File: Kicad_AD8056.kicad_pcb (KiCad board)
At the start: 2 copper layers, 63.5 x 70.9 mm, 10 parts, among them J1 Conn_Coaxial, J2 Screw_Terminal_01x03, J3 Conn_Coaxial, J4 Conn_01x01_Pin, J5 Conn_01x01_Pin, J6 Conn_01x01_Pin, U1 AD8056AR

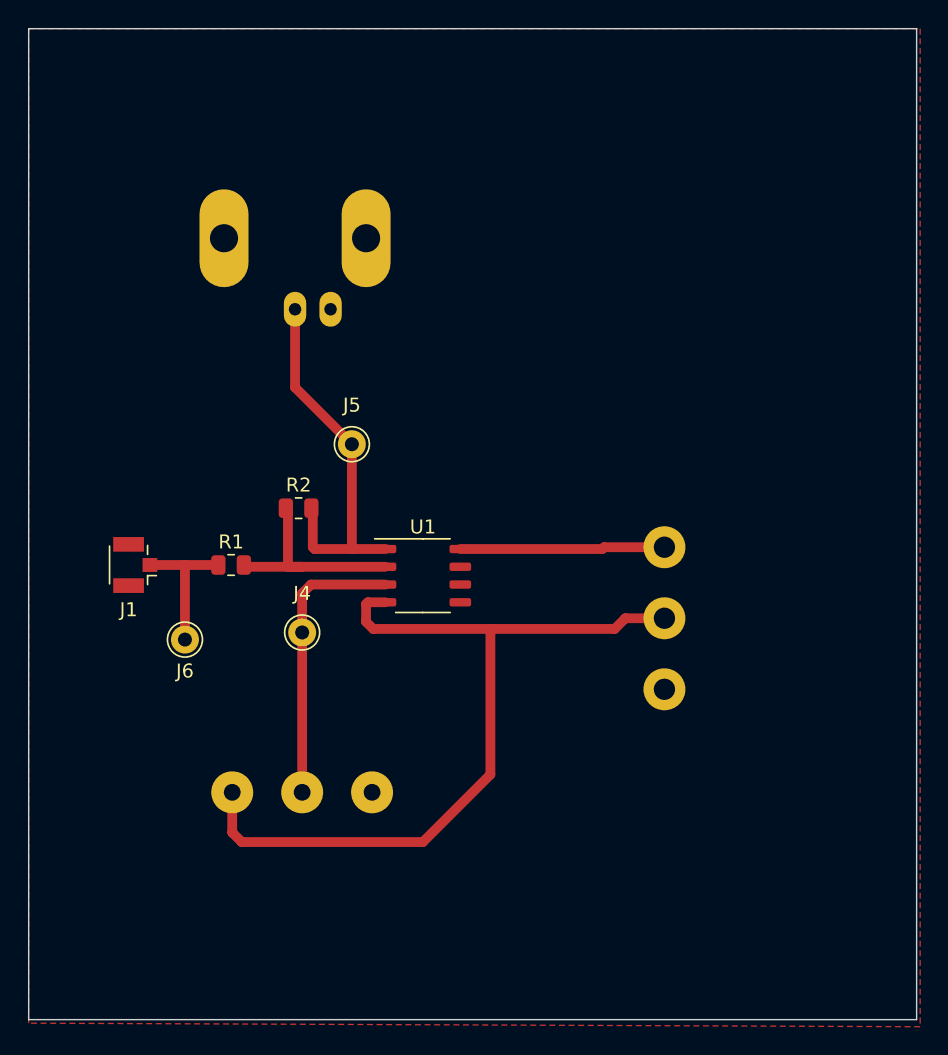
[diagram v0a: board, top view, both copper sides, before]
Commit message: add new pcb prototype
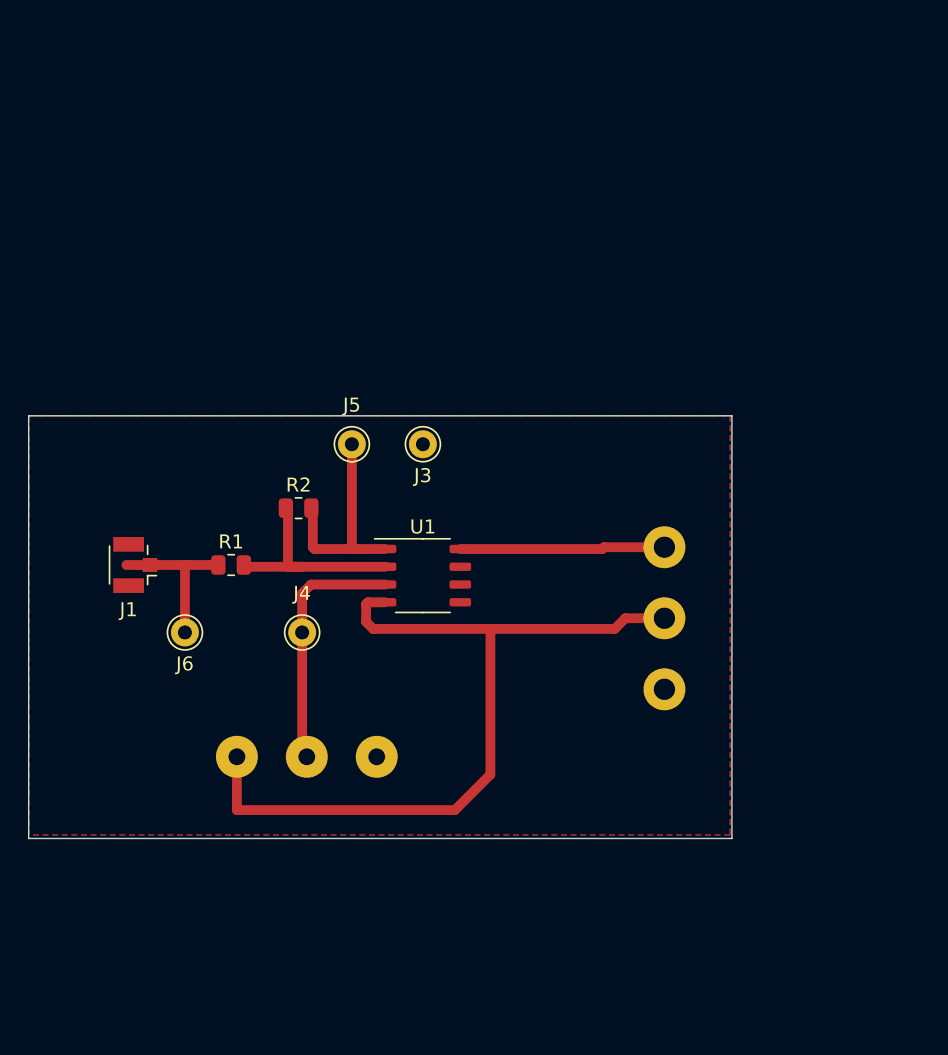
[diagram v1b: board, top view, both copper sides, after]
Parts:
- J3: value Conn_Coaxial -> Conn_01x01_Pin; footprint Connector_Coaxial:BNC_Amphenol_B6252HB-NPP3G-50_Horizontal -> Connector_Pin:Pin_D1.0mm_L10.0mm; moved to F.Cu
- moved J3 13.3 mm to (91.4, 42.4), turned to 0 degrees
- moved RV1 2.56 mm to (88.1, 64.8)
- moved J6 0.51 mm to (74.4, 55.9)
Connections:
- J3 pad 1: Net-(J3-In) -> GND
- J5 pad 1: Net-(J3-In) -> Net-(J5-Pin_1)
- R2 pad 2: Net-(J3-In) -> Net-(J5-Pin_1)
- U1 pad 1: Net-(J3-In) -> Net-(J5-Pin_1)
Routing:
- net Net-(J3-In): track 26.9 -> 0.00 mm
- net Net-(J5-Pin_1): track 0.00 -> 15.6 mm
- net Net-(J4-Pin_1): track 20.4 -> 18.0 mm
- net Net-(J1-In): track 10.2 -> 11.9 mm
- net -5V: track 58.6 -> 58.0 mm
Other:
- board size 63.5 x 70.9 mm -> 50.3 x 30.2 mm

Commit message: new pcb prototype №1
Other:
- board size 50.3 x 30.2 mm -> 44.8 x 30.2 mm
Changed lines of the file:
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@@
     )
   )
-  (gr_rect (start 63.246 40.386) (end 113.538 70.612)
+  (gr_rect (start 68.707 40.386) (end 113.538 70.612)
     (stroke (width 0.1) (type default)) (fill none) (layer "Edge.Cuts"))
   (segment (start 74.422 51.054) (end 71.916 51.054) (width 0.7) (layer "F.Cu") (net 1))
+  (segment (start 71.916 51.054) (end 70.485 51.054) (width 0.7) (layer "F.Cu") (net 1))
   (segment (start 76.8115 51.054) (end 74.422 51.054) (width 0.7) (layer "F.Cu") (net 1))
   (segment (start 74.422 51.054) (end 74.422 56.388) (width 0.7) (layer "F.Cu") (net 1))
-  (segment (start 71.916 51.054) (end 70.231 51.054) (width 0.7) (layer "F.Cu") (net 1))
   (segment (start 104.394 49.784) (end 108.712 49.784) (width 0.7) (layer "F.Cu") (net 3))
   (segment (start 104.267 49.911) (end 104.394 49.784) (width 0.7) (layer "F.Cu") (net 3))
@@
         (xy 113.411 40.386)
         (xy 113.411 70.358)
-        (xy 63.246 70.358)
-        (xy 63.246 40.386)
+        (xy 68.707 70.612)
+        (xy 68.707 40.386)
       )
     )
